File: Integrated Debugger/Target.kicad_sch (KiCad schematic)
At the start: 7 parts, among them J3 FPC socket 10P, J4 20021521-00010T1LF, Q1 NMOS DMN2991UDA-7B, SW2 RESET, U3 TXB0106RGY

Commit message: Debugger 1.1.2 production files
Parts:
- RN1: footprint Picoballoon Passives:Resistor Pack YC248-JR-07100RL -> Picoballoon Passives:Resistor 0402x8
- U3: footprint Picoballoon ICs:Texas_RGY_R-PVQFN-N16_EP2.05x2.55mm -> Picoballoon ICs:PVQFN-N16
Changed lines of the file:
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@@
 	(title_block
 		(title "Target")
-		(date "2025-11-01")
-		(rev "1.1.1")
+		(date "2025-11-03")
+		(rev "1.1.2")
 	)
 	(rectangle
@@
 			)
 		)
-		(property "Footprint" "Picoballoon Passives:Resistor Pack YC248-JR-07100RL"
+		(property "Footprint" "Picoballoon Passives:Resistor 0402x8"
 			(at 31.75 122.428 90)
 			(effects
@@
 			)
 		)
-		(property "Footprint" "Picoballoon Passives:Resistor Pack YC248-JR-07100RL"
+		(property "Footprint" "Picoballoon Passives:Resistor 0402x8"
 			(at 55.88 46.482 90)
 			(effects
@@
 			)
 		)
-		(property "Footprint" "Picoballoon Passives:Resistor Pack YC248-JR-07100RL"
+		(property "Footprint" "Picoballoon Passives:Resistor 0402x8"
 			(at 55.88 41.402 90)
 			(effects
@@
 			)
 		)
-		(property "Footprint" "Picoballoon Passives:Resistor Pack YC248-JR-07100RL"
+		(property "Footprint" "Picoballoon Passives:Resistor 0402x8"
 			(at 55.88 38.862 90)
 			(effects
@@
 			)
 		)
-		(property "Footprint" "Picoballoon Passives:Resistor Pack YC248-JR-07100RL"
+		(property "Footprint" "Picoballoon Passives:Resistor 0402x8"
 			(at 55.88 33.782 90)
 			(effects
@@
 			)
 		)
-		(property "Footprint" "Picoballoon Passives:Resistor Pack YC248-JR-07100RL"
+		(property "Footprint" "Picoballoon Passives:Resistor 0402x8"
 			(at 55.88 43.942 90)
 			(effects
@@
 			)
 		)
-		(property "Footprint" "Picoballoon Passives:Resistor Pack YC248-JR-07100RL"
+		(property "Footprint" "Picoballoon Passives:Resistor 0402x8"
 			(at 55.88 36.322 90)
 			(effects
@@
 			)
 		)
-		(property "Footprint" "Picoballoon ICs:Texas_RGY_R-PVQFN-N16_EP2.05x2.55mm"
+		(property "Footprint" "Picoballoon ICs:PVQFN-N16"
 			(at 35.56 55.88 0)
 			(effects

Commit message: IDBG schematic
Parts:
- removed SW2: RESET, Picoballoon Mechanical & Misc:Button GT-TC029B-H025-L1N, symbol Picoballoon Mechanical & Misc:Switch SPST
- added C18, C19: 100nF, Picoballoon Passives:Capacitor 0201, symbol Picoballoon Passives:Capacitor
- added D12: PUSB3AB6Z, Picoballoon ICs:XSON-7, symbol Picoballoon Passives:TVS array 6
- added unit 7 of RN1
- added SW5: YTS1T0161AWJ00, Picoballoon Mechanical & Misc:SMD-4P 4.2x3.2mm, symbol Picoballoon Mechanical & Misc:GT-TC048D-H025-L1
- J3: footprint Picoballoon Mechanical & Misc:FPC connector FPC-05F-10PH20 -> Picoballoon Mechanical & Misc:FH28-10S-0.5SH(05); JLCPCB Part # C2856798 -> (none); LCSC Part # C2856798 -> C598018; MPN FPC-05F-10PH20 -> FH28-10S-0.5SH(05)
- J4: JLCPCB Part # C2972785 -> (none)
- Q1: value NMOS DMN2991UDA-7B -> DMN31D5UDA-7B; JLCPCB Part # C2937136 -> (none); LCSC Part # C2937136 -> C17642742; MPN DMN2991UDA-7B -> DMN31D5UDA-7B
- R13: JLCPCB Part # C717002 -> (none)
- RN1: JLCPCB Part # C695200 -> (none)
- U3: JLCPCB Part # C2652978 -> (none)
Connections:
- net V_TARGET is gone; now on net VDD_TG: J3.1 (Pin_1), J4.1 (VCC)
- net GND: now also C18.2, C19.2, D12.2 (A), SW5.4
- net tRXD: now also D12.1 (K)
- net tTCK: now also D12.3 (K)
- net tTDI: now also D12.5 (K)
- net tTDO: now also D12.6 (K)
- net tTMS: now also D12.5 (K)
- net tTXD: now also D12.7 (K)
- net xRST: now also SW5.2
- net +3.3V renamed VDD_3V3
- net VDD_3V3: now also C19.1
- net TARGET renamed VDD_TG
- net VDD_TG: now also J4.10 (SOLAR), RN1.10 (R7.2)
- net V_AUX renamed VDD_AUX
- net VDD_AUX: no longer J4.10 (SOLAR)
- net xTPWR: no longer names the net of U3.15 (V_{CCB})
- net xTPWR: now also C18.1, RN1.7 (R7.1)
- no-connect marks 0 -> 2
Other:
- note added: "FPC TARGET CONNECTOR"
- note added: "IDC 1.27{dblquote} TARGET CONNECTOR"
- note added: "TARGET LEVEL SHIFTER"
- note removed: "FPC TARGET"
- note removed: "HOST <-> TARGET LEVEL SHIFTER"
- note removed: "MANUAL TARGET RESET"
- note removed: "PB-CONN TARGET"
- moved on the sheet: J3, J4, Q1, R13, RN1A, RN1B, RN1C, RN1D, RN1E, RN1F, RN1H, U3

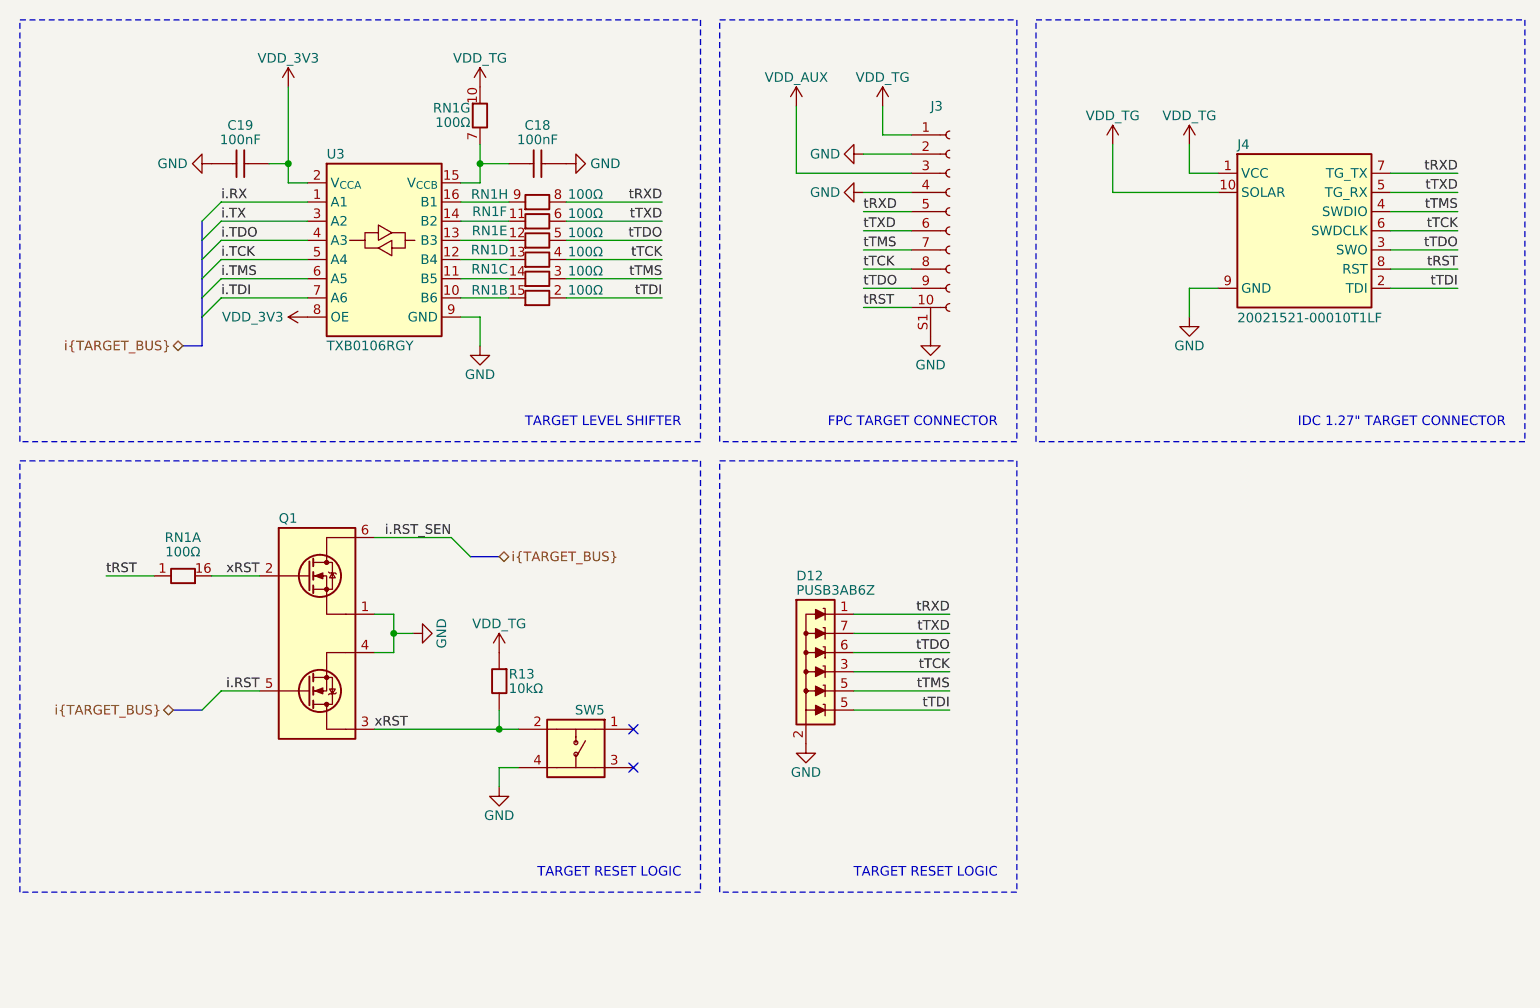
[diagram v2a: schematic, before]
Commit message: Integrated debugger PCB
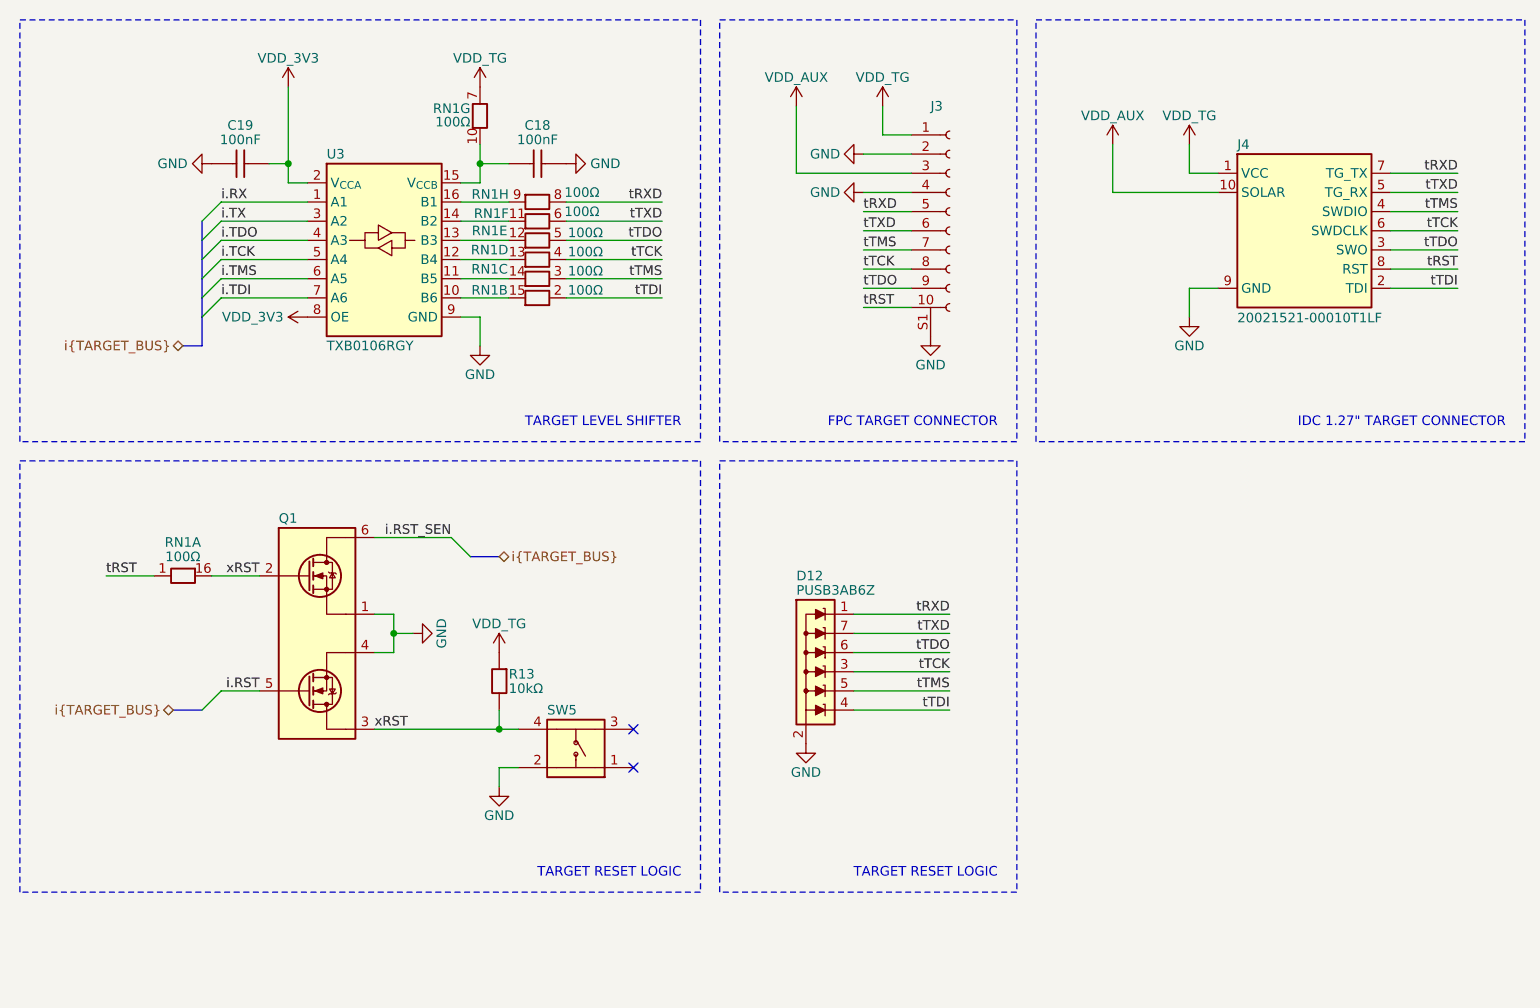
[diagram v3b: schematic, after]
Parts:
- SW5: value YTS1T0161AWJ00 -> RESET
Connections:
- net GND: now also SW5.2; no longer SW5.4
- net VDD_AUX: now also J4.10 (SOLAR)
- net VDD_TG: now also RN1.7 (R7.1); no longer J4.10 (SOLAR), RN1.10 (R7.2)
- net tTDI: now also D12.4 (K); no longer D12.5 (K)
- net xRST: now also SW5.4; no longer SW5.2
- net at C18.1, U3.15 (V_{CCB}): now also RN1.10 (R7.2); no longer RN1.7 (R7.1)
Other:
- moved on the sheet: SW5
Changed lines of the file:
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@@
 		(lib_id "Picoballoon Passives:Resistor array 8")
 		(at 26.67 78.74 270)
-		(mirror x)
 		(unit 1)
 		(exclude_from_sim no)
@@
 		(dnp no)
 		(property "Reference" "RN1"
-			(at 26.67 73.66 90)
+			(at 26.67 74.295 90)
 			(effects
 				(font
@@
 		)
 		(property "Value" "100Ω"
-			(at 26.67 75.565 90)
+			(at 26.67 76.2 90)
 			(effects
 				(font
@@
 		)
 		(property "Footprint" "Picoballoon Passives:Resistor 0402x8"
-			(at 26.67 80.772 90)
+			(at 26.67 76.708 90)
 			(effects
 				(font
@@
 		)
 		(property "Description" "8 resistor network, parallel topology, split"
-			(at 21.59 71.12 90)
+			(at 21.59 86.36 90)
 			(effects
 				(font
@@
 		(pin "1"
 		)
-		(pin "5"
+		(pin "4"
 		)
 		(pin "5"
@@
 		(lib_id "Picoballoon Passives:Resistor array 8")
 		(at 73.66 29.21 90)
+		(mirror x)
 		(unit 8)
 		(exclude_from_sim no)
@@
 		(dnp no)
 		(property "Reference" "RN1"
-			(at 67.31 28.194 90)
-			(effects
-				(font
-					(size 1.27 1.27)
-				)
+			(at 69.85 28.194 90)
+			(effects
+				(font
+					(size 1.27 1.27)
+				)
+				(justify left)
 			)
 		)
 		(property "Value" "100Ω"
-			(at 80.01 28.194 90)
-			(effects
-				(font
-					(size 1.27 1.27)
-				)
+			(at 77.216 27.94 90)
+			(effects
+				(font
+					(size 1.27 1.27)
+				)
+				(justify right)
 			)
 		)
 		(property "Footprint" "Picoballoon Passives:Resistor 0402x8"
-			(at 73.66 31.242 90)
+			(at 73.66 27.178 90)
 			(effects
 				(font
@@
 		)
 		(property "Description" "8 resistor network, parallel topology, split"
-			(at 78.74 21.59 90)
+			(at 78.74 36.83 90)
 			(effects
 				(font
@@
 					(reference "RN1")
 					(unit 8)
+				)
+			)
+		)
+	)
+	(symbol
+		(lib_id "Picoballoon Power Symbols:+3.3V")
+		(at 149.86 21.59 0)
+		(unit 1)
+		(exclude_from_sim no)
+		(in_bom yes)
+		(on_board yes)
+		(dnp no)
+		(property "Reference" "#PWR023"
+			(at 149.86 25.4 0)
+			(effects
+				(font
+					(size 1.27 1.27)
+				)
+				(hide yes)
+			)
+		)
+		(property "Value" "VDD_AUX"
+			(at 149.86 17.78 0)
+			(effects
+				(font
+					(size 1.27 1.27)
+				)
+			)
+		)
+		(property "Footprint" ""
+			(at 149.86 21.59 0)
+			(effects
+				(font
+					(size 1.27 1.27)
+				)
+				(hide yes)
+			)
+		)
+		(property "Datasheet" ""
+			(at 149.86 21.59 0)
+			(effects
+				(font
+					(size 1.27 1.27)
+				)
+				(hide yes)
+			)
+		)
+		(property "Description" ""
+			(at 149.86 21.59 0)
+			(effects
+				(font
+					(size 1.27 1.27)
+				)
+				(hide yes)
+			)
+		)
+		(pin "1"
+		)
+		(instances
+			(project "Integrated Debugger"
+				(path "/ce538ebe-fda9-4af3-9f8c-9fd5bf58f0e4/d9cee7b3-2b2b-4107-bac3-796b154ca54d"
+					(reference "#PWR023")
+					(unit 1)
 				)
 			)
@@
 		(dnp no)
 		(property "Reference" "RN1"
-			(at 67.31 30.48 90)
-			(effects
-				(font
-					(size 1.27 1.27)
-				)
+			(at 69.85 30.734 90)
+			(effects
+				(font
+					(size 1.27 1.27)
+				)
+				(justify left)
 			)
 		)
 		(property "Value" "100Ω"
-			(at 80.01 30.734 90)
-			(effects
-				(font
-					(size 1.27 1.27)
-				)
+			(at 77.216 30.48 90)
+			(effects
+				(font
+					(size 1.27 1.27)
+				)
+				(justify right)
 			)
 		)
@@
 		(lib_id "Picoballoon Passives:Resistor array 8")
 		(at 66.04 17.78 0)
+		(mirror x)
 		(unit 7)
 		(exclude_from_sim no)
@@
 		(dnp no)
 		(property "Reference" "RN1"
-			(at 64.77 16.764 0)
+			(at 64.77 16.8275 0)
 			(effects
 				(font
@@
 		)
 		(property "Value" "100Ω"
-			(at 64.77 18.669 0)
+			(at 64.77 18.6055 0)
 			(effects
 				(font
@@
 		)
 		(property "Description" "8 resistor network, parallel topology, split"
-			(at 73.66 22.86 90)
+			(at 73.66 12.7 90)
 			(effects
 				(font
@@
 				(path "/ce538ebe-fda9-4af3-9f8c-9fd5bf58f0e4/d9cee7b3-2b2b-4107-bac3-796b154ca54d"
 					(reference "#PWR014")
-					(unit 1)
-				)
-			)
-		)
-	)
-	(symbol
-		(lib_id "Picoballoon Power Symbols:+3.3V")
-		(at 149.86 21.59 0)
-		(unit 1)
-		(exclude_from_sim no)
-		(in_bom yes)
-		(on_board yes)
-		(dnp no)
-		(property "Reference" "#PWR023"
-			(at 149.86 25.4 0)
-			(effects
-				(font
-					(size 1.27 1.27)
-				)
-				(hide yes)
-			)
-		)
-		(property "Value" "VDD_TG"
-			(at 149.86 17.78 0)
-			(effects
-				(font
-					(size 1.27 1.27)
-				)
-			)
-		)
-		(property "Footprint" ""
-			(at 149.86 21.59 0)
-			(effects
-				(font
-					(size 1.27 1.27)
-				)
-				(hide yes)
-			)
-		)
-		(property "Datasheet" ""
-			(at 149.86 21.59 0)
-			(effects
-				(font
-					(size 1.27 1.27)
-				)
-				(hide yes)
-			)
-		)
-		(property "Description" ""
-			(at 149.86 21.59 0)
-			(effects
-				(font
-					(size 1.27 1.27)
-				)
-				(hide yes)
-			)
-		)
-		(pin "1"
-		)
-		(instances
-			(project "Integrated Debugger"
-				(path "/ce538ebe-fda9-4af3-9f8c-9fd5bf58f0e4/d9cee7b3-2b2b-4107-bac3-796b154ca54d"
-					(reference "#PWR023")
 					(unit 1)
 				)
@@
 	(symbol
 		(lib_id "Picoballoon Mechanical & Misc:GT-TC048D-H025-L1")
-		(at 78.74 102.87 0)
-		(mirror y)
+		(at 78.74 100.33 180)
 		(unit 1)
 		(exclude_from_sim no)
@@
 		(dnp no)
 		(property "Reference" "SW5"
-			(at 82.55 96.52 0)
-			(effects
-				(font
-					(size 1.27 1.27)
-				)
-				(justify left)
-			)
-		)
-		(property "Value" "YTS1T0161AWJ00"
-			(at 79.248 107.442 0)
+			(at 74.93 96.52 0)
+			(effects
+				(font
+					(size 1.27 1.27)
+				)
+				(justify right)
+			)
+		)
+		(property "Value" "RESET"
+			(at 79.248 95.758 0)
 			(effects
 				(font
@@
 		)
 		(property "Footprint" "Picoballoon Mechanical & Misc:SMD-4P 4.2x3.2mm"
-			(at 78.74 111.76 0)
+			(at 78.74 91.44 0)
 			(effects
 				(font
@@
 		)
 		(property "Datasheet" "https://www.lcsc.com/datasheet/C2985732.pdf"
-			(at 78.74 114.3 0)
+			(at 78.74 88.9 0)
 			(effects
 				(font
@@
 		)
 		(property "Description" "Without Bracket 4.2mm 12V 3.2mm Oval Button No SPST 50mA SMD-4P,4.2x3.2mm Tactile Switches ROHS"
-			(at 78.74 116.84 0)
+			(at 78.74 86.36 0)
 			(effects
 				(font
@@
 		)
 		(property "MPN" "YTS1T0161AWJ00"
-			(at 78.74 119.38 0)
+			(at 78.74 83.82 0)
 			(effects
 				(font
@@
 		)
 		(property "LCSC Part #" "C2985732"
-			(at 78.74 121.92 0)
-			(effects
-				(font
+			(at 78.74 81.28 0)
+			(effects
+				(font
